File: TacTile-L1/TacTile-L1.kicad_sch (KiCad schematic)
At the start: 10 parts, among them J1 Conn_01x02, J2 Conn_01x02

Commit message: Added some footprints for laser boards
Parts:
- J1: footprint (none) -> Connector_PinHeader_2.00mm:PinHeader_1x02_P2.00mm_Horizontal
- J2: footprint (none) -> Connector_PinSocket_2.00mm:PinSocket_1x02_P2.00mm_Horizontal
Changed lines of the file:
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@@
       (effects (font (size 1.27 1.27)) (justify left))
     )
-    (property "Footprint" "" (at 29.21 93.98 0)
+    (property "Footprint" "Connector_PinSocket_2.00mm:PinSocket_1x02_P2.00mm_Horizontal" (at 29.21 93.98 0)
       (effects (font (size 1.27 1.27)) hide)
     )
@@
       (effects (font (size 1.27 1.27)) (justify right))
     )
-    (property "Footprint" "" (at 25.4 17.78 0)
-      (effects (font (size 1.27 1.27)) hide)
-    )
+    (property "Footprint" "Connector_PinHeader_2.00mm:PinHeader_1x02_P2.00mm_Horizontal" (at 25.4 17.78 0)
+      (effects (font (size 1.27 1.27)) hide)
+    )

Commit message: Finished L1 Board
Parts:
- LD1, LD2, LD3, LD4, LD5, LD6, LD7, LD8: footprint (none) -> TacTile:Laser_Diode
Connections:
- net VCC: now reaches J1.1 (Pin_1), LD1.1 (K), LD2.1 (K), LD3.1 (K), LD4.1 (K), LD5.1 (K), LD6.1 (K), LD7.1 (K), LD8.1 (K)
- net VCC: now also J2.1 (Pin_1); no longer J2.2 (Pin_2)
- net GND: now reaches J1.2 (Pin_2), LD1.2 (A), LD2.2 (A), LD3.2 (A), LD4.2 (A), LD5.2 (A), LD6.2 (A), LD7.2 (A), LD8.2 (A)
- net GND: now also J2.2 (Pin_2); no longer J2.1 (Pin_1)
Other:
- moved on the sheet: J2
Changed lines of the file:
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@@
+    (stroke (width 0) (type default))
+  )
+  (wire (pts (xy 26.67 88.9) (xy 26.67 96.52))
     (stroke (width 0) (type default))
   )
@@
     (stroke (width 0) (type default))
   )
+  (wire (pts (xy 29.21 88.9) (xy 29.21 96.52))
+    (stroke (width 0) (type default))
+  )
   (wire (pts (xy 33.02 43.18) (xy 33.02 50.8))
     (stroke (width 0) (type default))
@@
     (stroke (width 0) (type default))
   )
+  (label "VCC" (at 20.32 54.61 180) (fields_autoplaced)
+    (effects (font (size 1.27 1.27)) (justify right bottom))
+  )
+  (label "GND" (at 33.02 54.61 0) (fields_autoplaced)
+    (effects (font (size 1.27 1.27)) (justify left bottom))
+  )
   (symbol (lib_id "Device:D_Laser_1C2A") (at 27.94 58.42 0) (unit 1)
     (in_bom yes) (on_board yes) (dnp no)
@@
       (effects (font (size 1.27 1.27)))
     )
-    (property "Footprint" "" (at 25.4 59.055 0)
+    (property "Footprint" "TacTile:Laser_Diode" (at 25.4 59.055 0)
       (effects (font (size 1.27 1.27)) hide)
     )
@@
     )
   )
-  (symbol (lib_id "Connector_Generic:Conn_01x02") (at 29.21 93.98 270) (unit 1)
+  (symbol (lib_id "Connector_Generic:Conn_01x02") (at 26.67 91.44 90) (unit 1)
     (in_bom yes) (on_board yes) (dnp no) (fields_autoplaced)
-    (property "Reference" "J2" (at 31.75 93.345 90)
-      (effects (font (size 1.27 1.27)) (justify left))
-    )
-    (property "Value" "Conn_01x02" (at 31.75 95.885 90)
-      (effects (font (size 1.27 1.27)) (justify left))
-    )
-    (property "Footprint" "Connector_PinSocket_2.00mm:PinSocket_1x02_P2.00mm_Horizontal" (at 29.21 93.98 0)
-      (effects (font (size 1.27 1.27)) hide)
-    )
-    (property "Datasheet" "~" (at 29.21 93.98 0)
+    (property "Reference" "J2" (at 31.75 90.805 90)
+      (effects (font (size 1.27 1.27)) (justify right))
+    )
+    (property "Value" "Conn_01x02" (at 31.75 93.345 90)
+      (effects (font (size 1.27 1.27)) (justify right))
+    )
+    (property "Footprint" "Connector_PinSocket_2.00mm:PinSocket_1x02_P2.00mm_Horizontal" (at 26.67 91.44 0)
+      (effects (font (size 1.27 1.27)) hide)
+    )
+    (property "Datasheet" "~" (at 26.67 91.44 0)
       (effects (font (size 1.27 1.27)) hide)
     )
@@
       (effects (font (size 1.27 1.27)))
     )
-    (property "Footprint" "" (at 25.4 31.115 0)
+    (property "Footprint" "TacTile:Laser_Diode" (at 25.4 31.115 0)
       (effects (font (size 1.27 1.27)) hide)
     )
@@
       (effects (font (size 1.27 1.27)))
     )
-    (property "Footprint" "" (at 25.4 36.195 0)
+    (property "Footprint" "TacTile:Laser_Diode" (at 25.4 36.195 0)
       (effects (font (size 1.27 1.27)) hide)
     )
@@
       (effects (font (size 1.27 1.27)))
     )
-    (property "Footprint" "" (at 25.4 66.675 0)
+    (property "Footprint" "TacTile:Laser_Diode" (at 25.4 66.675 0)
       (effects (font (size 1.27 1.27)) hide)
     )
@@
       (effects (font (size 1.27 1.27)))
     )
-    (property "Footprint" "" (at 25.4 43.815 0)
+    (property "Footprint" "TacTile:Laser_Diode" (at 25.4 43.815 0)
       (effects (font (size 1.27 1.27)) hide)
     )
@@
       (effects (font (size 1.27 1.27)))
     )
-    (property "Footprint" "" (at 25.4 51.435 0)
+    (property "Footprint" "TacTile:Laser_Diode" (at 25.4 51.435 0)
       (effects (font (size 1.27 1.27)) hide)
     )
@@
       (effects (font (size 1.27 1.27)))
     )
-    (property "Footprint" "" (at 25.4 84.455 0)
+    (property "Footprint" "TacTile:Laser_Diode" (at 25.4 84.455 0)
       (effects (font (size 1.27 1.27)) hide)
     )
@@
       (effects (font (size 1.27 1.27)))
     )
-    (property "Footprint" "" (at 25.4 75.565 0)
-      (effects (font (size 1.27 1.27)) hide)
-    )
+    (property "Footprint" "TacTile:Laser_Diode" (at 25.4 75.565 0)
+      (effects (font (size 1.27 1.27)) hide)
+    )

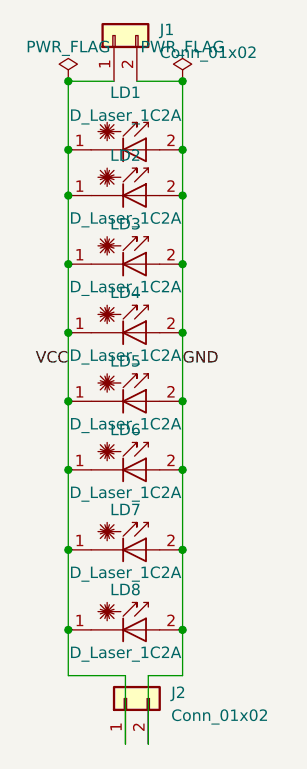
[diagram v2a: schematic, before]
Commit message: Finished enlarging pins on C, D, L1, L2
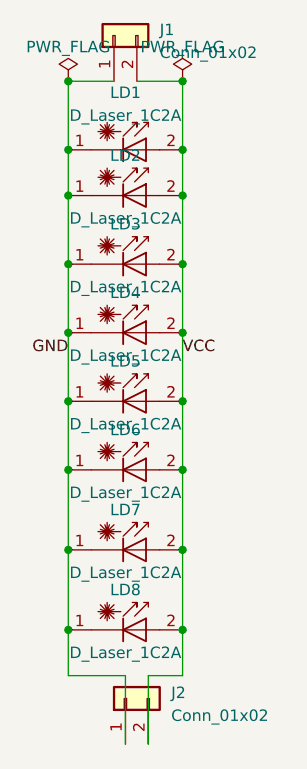
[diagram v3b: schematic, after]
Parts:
- J1: footprint Connector_PinHeader_2.00mm:PinHeader_1x02_P2.00mm_Horizontal -> Connector_PinSocket_2.54mm:PinSocket_1x02_P2.54mm_Horizontal
- J2: footprint Connector_PinSocket_2.00mm:PinSocket_1x02_P2.00mm_Horizontal -> Connector_PinHeader_2.54mm:PinHeader_1x02_P2.54mm_Horizontal
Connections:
- net GND: now also J1.1 (Pin_1), J2.1 (Pin_1), LD1.1 (K), LD2.1 (K), LD3.1 (K), LD4.1 (K), LD5.1 (K), LD6.1 (K), LD7.1 (K), LD8.1 (K); no longer J1.2 (Pin_2), J2.2 (Pin_2), LD1.2 (A), LD2.2 (A), LD3.2 (A), LD4.2 (A), LD5.2 (A), LD6.2 (A), LD7.2 (A), LD8.2 (A)
- net VCC: now also J1.2 (Pin_2), J2.2 (Pin_2), LD1.2 (A), LD2.2 (A), LD3.2 (A), LD4.2 (A), LD5.2 (A), LD6.2 (A), LD7.2 (A), LD8.2 (A); no longer J1.1 (Pin_1), J2.1 (Pin_1), LD1.1 (K), LD2.1 (K), LD3.1 (K), LD4.1 (K), LD5.1 (K), LD6.1 (K), LD7.1 (K), LD8.1 (K)
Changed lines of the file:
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@@
     (stroke (width 0) (type default))
   )
-  (label "VCC" (at 20.32 54.61 180) (fields_autoplaced)
+  (label "VCC" (at 33.02 53.34 0) (fields_autoplaced)
+    (effects (font (size 1.27 1.27)) (justify left bottom))
+  )
+  (label "GND" (at 20.32 53.34 180) (fields_autoplaced)
     (effects (font (size 1.27 1.27)) (justify right bottom))
   )
-  (label "GND" (at 33.02 54.61 0) (fields_autoplaced)
-    (effects (font (size 1.27 1.27)) (justify left bottom))
-  )
   (symbol (lib_id "Device:D_Laser_1C2A") (at 27.94 58.42 0) (unit 1)
     (in_bom yes) (on_board yes) (dnp no)
@@
       (effects (font (size 1.27 1.27)) (justify right))
     )
-    (property "Footprint" "Connector_PinSocket_2.00mm:PinSocket_1x02_P2.00mm_Horizontal" (at 26.67 91.44 0)
+    (property "Footprint" "Connector_PinHeader_2.54mm:PinHeader_1x02_P2.54mm_Horizontal" (at 26.67 91.44 0)
       (effects (font (size 1.27 1.27)) hide)
     )
@@
       (effects (font (size 1.27 1.27)) (justify right))
     )
-    (property "Footprint" "Connector_PinHeader_2.00mm:PinHeader_1x02_P2.00mm_Horizontal" (at 25.4 17.78 0)
-      (effects (font (size 1.27 1.27)) hide)
-    )
+    (property "Footprint" "Connector_PinSocket_2.54mm:PinSocket_1x02_P2.54mm_Horizontal" (at 25.4 17.78 0)
+      (effects (font (size 1.27 1.27)) hide)
+    )

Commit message: Created connector boards for laser matrix
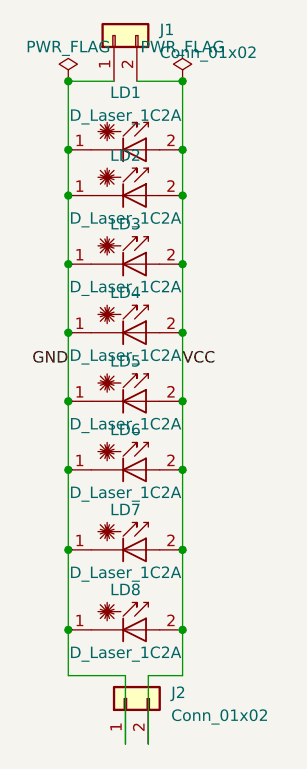
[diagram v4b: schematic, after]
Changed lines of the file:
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@@
     (stroke (width 0) (type default))
   )
-  (label "VCC" (at 33.02 53.34 0) (fields_autoplaced)
+  (label "VCC" (at 33.02 54.61 0) (fields_autoplaced)
     (effects (font (size 1.27 1.27)) (justify left bottom))
   )
-  (label "GND" (at 20.32 53.34 180) (fields_autoplaced)
+  (label "GND" (at 20.32 54.61 180) (fields_autoplaced)
     (effects (font (size 1.27 1.27)) (justify right bottom))
   )
